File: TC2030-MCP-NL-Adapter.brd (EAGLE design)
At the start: 35.8 x 55.5 mm, 11 parts, among them J1 95501-6669

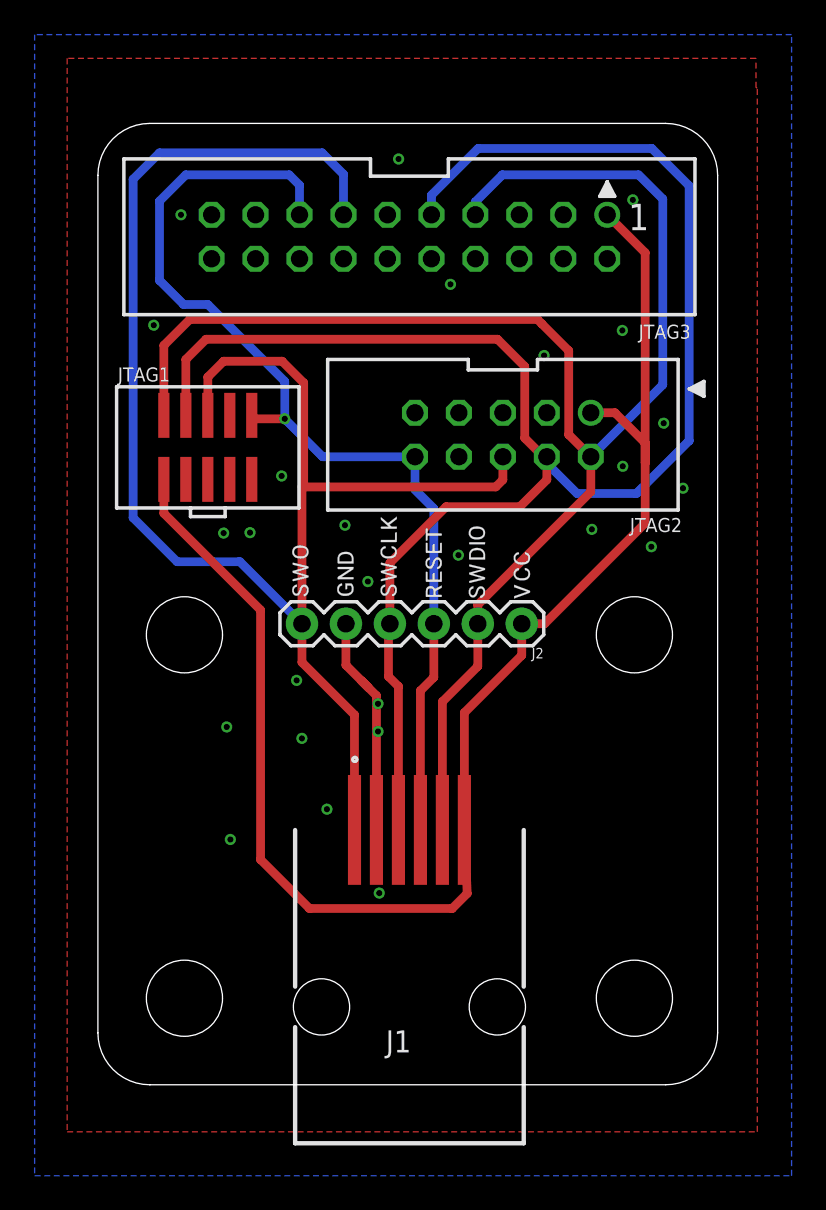
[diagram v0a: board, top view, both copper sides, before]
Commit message: update RJ12 variant with 6p connector
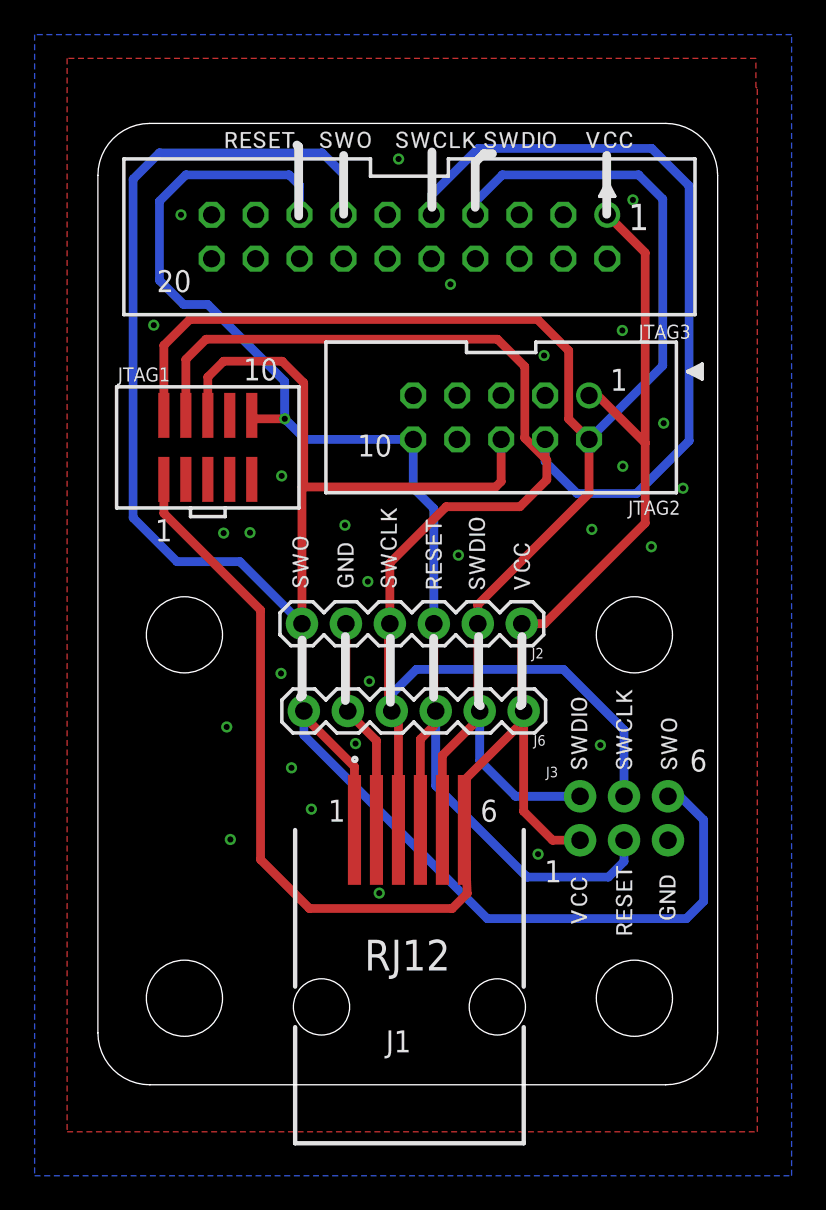
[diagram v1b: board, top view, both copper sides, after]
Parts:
- added J3: (no value), SparkFun-Connectors:2X3-NS
- added J6: (no value), SparkFun-Connectors:1X06
- added U$10, U$14: (no value), output:VCC0
- added U$11, U$16: (no value), output:SWCLK0
- added U$12, U$7: (no value), output:SWO0
- added U$13, U$9: (no value), output:RESET0
- added U$15: (no value), output:GND0
- added U$17, U$8: (no value), output:SWDIO0
- moved JTAG2 1.00 mm to (23.3, 38.6)
- moved U$1 0.50 mm to (11.7, 28.0)
- moved U$2 0.50 mm to (14.3, 28.0)
- moved U$3 0.50 mm to (16.8, 28.0)
- moved U$4 0.50 mm to (19.4, 27.9)
- moved U$5 0.50 mm to (21.9, 27.9)
- moved U$6 0.50 mm to (24.5, 27.9)
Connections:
- net GND: now also J3.5, J6.5
- net RESET: now also J3.3, J6.3
- net SWCLK: now also J3.4, J6.4
- net SWDIO: now also J3.2, J6.2
- net SWO: now also J3.6, J6.6
- net VCC: now also J3.1, J6.1
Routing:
- net SWO: track 96.4 -> 134.2 mm
- net SWCLK: track 101.3 -> 123.6 mm
- net RESET: track 59.8 -> 79.5 mm
- net VCC: track 88.0 -> 97.2 mm
- net SWDIO: track 90.0 -> 98.6 mm
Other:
- board text added: "1"
- board text added: "10"
- board text added: "20"
- board text added: "6"
- board text added: "RJ12"
